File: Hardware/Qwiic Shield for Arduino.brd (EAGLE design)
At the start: 53.3 x 59.7 mm, 22 parts, among them Q1 BSS138, Q2 BSS138, U1 ARDUINO UNO

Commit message: Changed over to Sparkfun library from SparkX
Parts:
- J1, J10, J8, J9: value (none) -> Qwiic Right Angle; device SparkX:1X04_1MM_RA -> SparkFun-Connectors:1X04_1MM_RA
- U$2: value SPARKX-LOGO5 -> SFE_LOGO_NAME_FLAME.1_INCH; device SparkX:SPARKX-LARGE -> SparkFun-Aesthetics:SFE_LOGO_NAME_FLAME_.1
- moved U$2 6.48 mm to (33.0, 1.27)
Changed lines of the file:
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@@
 <grid distance="0.05" unitdist="inch" unit="inch" style="lines" multiple="1" display="yes" altdistance="0.005" altunitdist="inch" altunit="inch"/>
 <layers>
-<layer number="1" name="Top" color="4" fill="1" visible="no" active="yes"/>
+<layer number="1" name="Top" color="4" fill="1" visible="yes" active="yes"/>
 <layer number="2" name="Route2" color="1" fill="3" visible="no" active="no"/>
 <layer number="3" name="Route3" color="4" fill="3" visible="no" active="no"/>
@@
 <layer number="16" name="Bottom" color="1" fill="1" visible="yes" active="yes"/>
 <layer number="17" name="Pads" color="2" fill="1" visible="yes" active="yes"/>
-<layer number="18" name="Vias" color="2" fill="1" visible="yes" active="yes"/>
+<layer number="18" name="Vias" color="2" fill="1" visible="no" active="yes"/>
 <layer number="19" name="Unrouted" color="6" fill="1" visible="no" active="yes"/>
 <layer number="20" name="Dimension" color="15" fill="1" visible="yes" active="yes"/>
 <layer number="21" name="tPlace" color="16" fill="1" visible="yes" active="yes"/>
-<layer number="22" name="bPlace" color="14" fill="1" visible="no" active="yes"/>
+<layer number="22" name="bPlace" color="14" fill="1" visible="yes" active="yes"/>
 <layer number="23" name="tOrigins" color="15" fill="1" visible="yes" active="yes"/>
-<layer number="24" name="bOrigins" color="15" fill="1" visible="no" active="yes"/>
+<layer number="24" name="bOrigins" color="15" fill="1" visible="yes" active="yes"/>
 <layer number="25" name="tNames" color="7" fill="1" visible="no" active="yes"/>
 <layer number="26" name="bNames" color="7" fill="1" visible="no" active="yes"/>
@@
 <element name="FD1" library="SparkFun-Aesthetics" package="FIDUCIAL-1X2" value="FIDUCIAL1X2" x="52.07" y="5.08"/>
 <element name="FD2" library="SparkFun-Aesthetics" package="FIDUCIAL-1X2" value="FIDUCIAL1X2" x="3.81" y="57.15"/>
-<element name="J1" library="SparkX" package="1X04_1MM_RA" value="" x="15.24" y="5.08"/>
+<element name="J1" library="SparkFun-Connectors" package="1X04_1MM_RA" value="Qwiic Right Angle" x="15.24" y="5.08" smashed="yes">
+<attribute name="PROD_ID" value="CONN-13729" x="15.24" y="5.08" size="1.778" layer="27" display="off"/>
+<attribute name="VALUE" value="Qwiic Right Angle" x="15.24" y="5.08" size="1.778" layer="27" display="off"/>
+<attribute name="NAME" x="13.843" y="2.921" size="0.6096" layer="25" font="vector" ratio="20"/>
+<attribute name="VALUE" x="11.049" y="1.778" size="0.6096" layer="27" font="vector" ratio="20"/>
+</element>
 <element name="J2" library="SparkFun-Connectors" package="1X08_NO_SILK" value="" x="7.62" y="54.61" rot="R270">
 <attribute name="PROD_ID" value="CONN-08438" x="7.62" y="54.61" size="1.778" layer="27" font="vector" ratio="15" rot="R270" display="off"/>
@@
 </element>
 <element name="J6" library="SparkFun-Connectors" package="1X07_NO_SILK" value="" x="45.72" y="21.59" rot="R90"/>
-<element name="J8" library="SparkX" package="1X04_1MM_RA" value="" x="22.86" y="5.08"/>
-<element name="J9" library="SparkX" package="1X04_1MM_RA" value="" x="30.48" y="5.08"/>
-<element name="J10" library="SparkX" package="1X04_1MM_RA" value="" x="38.1" y="5.08"/>
-<element name="U$2" library="SparkX" package="SPARKX-LARGE" value="SPARKX-LOGO5" x="26.67" y="2.54" rot="MR0"/>
+<element name="J8" library="SparkFun-Connectors" package="1X04_1MM_RA" value="Qwiic Right Angle" x="22.86" y="5.08" smashed="yes">
+<attribute name="PROD_ID" value="CONN-13729" x="22.86" y="5.08" size="1.778" layer="27" display="off"/>
+<attribute name="VALUE" value="Qwiic Right Angle" x="22.86" y="5.08" size="1.778" layer="27" display="off"/>
+<attribute name="NAME" x="21.463" y="2.921" size="0.6096" layer="25" font="vector" ratio="20"/>
+<attribute name="VALUE" x="18.669" y="0.508" size="0.6096" layer="27" font="vector" ratio="20"/>
+</element>
+<element name="J9" library="SparkFun-Connectors" package="1X04_1MM_RA" value="Qwiic Right Angle" x="30.48" y="5.08" smashed="yes">
+<attribute name="PROD_ID" value="CONN-13729" x="30.48" y="5.08" size="1.778" layer="27" display="off"/>
+<attribute name="VALUE" value="Qwiic Right Angle" x="30.48" y="5.08" size="1.778" layer="27" display="off"/>
+<attribute name="NAME" x="29.083" y="2.921" size="0.6096" layer="25" font="vector" ratio="20"/>
+<attribute name="VALUE" x="26.289" y="1.778" size="0.6096" layer="27" font="vector" ratio="20"/>
+</element>
+<element name="J10" library="SparkFun-Connectors" package="1X04_1MM_RA" value="Qwiic Right Angle" x="38.1" y="5.08" smashed="yes">
+<attribute name="PROD_ID" value="CONN-13729" x="38.1" y="5.08" size="1.778" layer="27" display="off"/>
+<attribute name="VALUE" value="Qwiic Right Angle" x="38.1" y="5.08" size="1.778" layer="27" display="off"/>
+<attribute name="NAME" x="36.703" y="2.921" size="0.6096" layer="25" font="vector" ratio="20"/>
+<attribute name="VALUE" x="33.909" y="0.508" size="0.6096" layer="27" font="vector" ratio="20"/>
+</element>
+<element name="U$2" library="SparkFun-Aesthetics" package="SFE_LOGO_NAME_FLAME_.1" value="SFE_LOGO_NAME_FLAME.1_INCH" x="33.02" y="1.27" rot="MR0"/>
 <element name="U$3" library="SparkX" package="QWIIC_BOARD_MOUNT_HOLES" value="QWIIC_BOARD_OUTLINEH" x="26.67" y="22.86" rot="R90"/>
 <element name="U$1" library="SparkFun-Aesthetics" package="SFE_LOGO_NAME_.1" value="" x="0" y="1.27"/>

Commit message: Partially completed checklist, changes still need to be made
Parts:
- added LOGO2: REVISION, SparkFun-Aesthetics:REVISION
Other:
- board text added: "V01"
- board text removed: "X11"

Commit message: Completed checklist + pre-design review changes
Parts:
- added FD3, FD4: FIDUCIAL1X2, SparkFun-Aesthetics:FIDUCIAL-1X2
- moved LOGO2 31.9 mm to (2.54, -30.5)
- moved FRAME1 3.81 mm to (-8.89, -27.9)
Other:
- board text added: "A. England"
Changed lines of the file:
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@@
 <layer number="23" name="tOrigins" color="15" fill="1" visible="yes" active="yes"/>
 <layer number="24" name="bOrigins" color="15" fill="1" visible="yes" active="yes"/>
-<layer number="25" name="tNames" color="7" fill="1" visible="yes" active="yes"/>
-<layer number="26" name="bNames" color="7" fill="1" visible="yes" active="yes"/>
-<layer number="27" name="tValues" color="7" fill="1" visible="yes" active="yes"/>
-<layer number="28" name="bValues" color="7" fill="1" visible="yes" active="yes"/>
+<layer number="25" name="tNames" color="7" fill="1" visible="no" active="yes"/>
+<layer number="26" name="bNames" color="7" fill="1" visible="no" active="yes"/>
+<layer number="27" name="tValues" color="7" fill="1" visible="no" active="yes"/>
+<layer number="28" name="bValues" color="7" fill="1" visible="no" active="yes"/>
 <layer number="29" name="tStop" color="7" fill="3" visible="yes" active="yes"/>
 <layer number="30" name="bStop" color="7" fill="6" visible="yes" active="yes"/>
@@
 <text x="47.371" y="3.81" size="1.524" layer="21" font="vector" ratio="15" align="center">Qwiic
 Shield</text>
-<text x="22.86" y="-24.13" size="1.778" layer="51" font="vector" ratio="15">N. Seidle</text>
+<text x="21.59" y="-27.94" size="1.778" layer="51" font="vector">N. Seidle</text>
 <wire x1="2.54" y1="0" x2="50.8" y2="0" width="0.2032" layer="20"/>
 <wire x1="0" y1="57.15" x2="2.54" y2="59.69" width="0.2032" layer="20"/>
@@
 <wire x1="53.34" y1="2.54" x2="50.8" y2="0" width="0.2032" layer="20"/>
 <wire x1="2.54" y1="0" x2="0" y2="2.54" width="0.2032" layer="20"/>
-<text x="48.26" y="57.785" size="1.524" layer="16" font="vector" ratio="20" rot="MR0" align="center">V01</text>
 <text x="5.207" y="54.61" size="1.016" layer="21" font="vector" ratio="15" align="center">RX</text>
 <text x="5.207" y="52.07" size="1.016" layer="21" font="vector" ratio="15" align="center">TX</text>
@@
 <text x="27.94" y="26.543" size="1.778" layer="22" font="vector" ratio="15" rot="MR90" align="center">5V</text>
 <text x="25.4" y="25.781" size="1.778" layer="22" font="vector" ratio="15" rot="MR90" align="center">GND</text>
-<text x="26.924" y="8.382" size="1.524" layer="22" font="vector" ratio="15" rot="MR0" align="center">3.3V I C Ports</text>
-<text x="25.781" y="8.636" size="1.016" layer="22" font="vector" ratio="15" rot="MR0">2</text>
 <text x="46.609" y="3.81" size="1.524" layer="22" font="vector" ratio="15" rot="MR0" align="center">Qwiic
 Shield</text>
@@
 <wire x1="17.78" y1="36.83" x2="22.86" y2="36.83" width="1.524" layer="30"/>
 <text x="7.366" y="0.508" size="1.778" layer="16" font="vector" ratio="15" rot="MR0">V01</text>
+<text x="21.59" y="-30.48" size="1.778" layer="51">A. England</text>
+<dimension x1="0" y1="0" x2="0" y2="59.69" x3="-6.35" y3="29.845" textsize="1.778" layer="47"/>
+<dimension x1="0" y1="57.15" x2="0" y2="59.69" x3="-2.54" y3="58.42" textsize="1.778" layer="47"/>
+<dimension x1="0" y1="0" x2="0" y2="2.54" x3="-2.54" y3="1.27" textsize="1.778" layer="47"/>
+<dimension x1="0" y1="0" x2="53.34" y2="0" x3="26.67" y3="-19.05" textsize="1.778" layer="47"/>
+<dimension x1="0" y1="0" x2="2.54" y2="0" x3="1.27" y3="-3.81" textsize="1.778" layer="47"/>
 </plain>
 <attributes>
@@
 <elements>
 <element name="U1" library="SparkFun-Boards" package="UNO_R3_SHIELD_NOLABELS" value="ARDUINO UNO" x="0" y="0"/>
-<element name="FRAME1" library="SparkFun-Aesthetics" package="CREATIVE_COMMONS" value="FRAME-LETTER" x="-8.89" y="-24.13"/>
+<element name="FRAME1" library="SparkFun-Aesthetics" package="CREATIVE_COMMONS" value="FRAME-LETTER" x="-8.89" y="-27.94"/>
 <element name="Q1" library="SparkFun-DiscreteSemi" package="SOT23-3" value="BSS138" x="50.8" y="12.7" smashed="yes">
 <attribute name="NAME" x="49.9745" y="14.478" size="0.8128" layer="25"/>
@@
 <element name="U$3" library="SparkX" package="QWIIC_BOARD_MOUNT_HOLES" value="QWIIC_BOARD_OUTLINEH" x="26.67" y="22.86" rot="R90"/>
 <element name="U$1" library="SparkFun-Aesthetics" package="SFE_LOGO_NAME_.1" value="" x="0" y="1.27"/>
-<element name="LOGO2" library="SparkFun-Aesthetics" package="REVISION" value="REVISION" x="-29.21" y="-27.94"/>
+<element name="LOGO2" library="SparkFun-Aesthetics" package="REVISION" value="REVISION" x="2.54" y="-30.48"/>
+<element name="FD3" library="SparkFun-Aesthetics" package="FIDUCIAL-1X2" value="FIDUCIAL1X2" x="52.07" y="5.08" rot="MR0"/>
+<element name="FD4" library="SparkFun-Aesthetics" package="FIDUCIAL-1X2" value="FIDUCIAL1X2" x="3.81" y="57.15" rot="MR0"/>
 </elements>
 <signals>
@@
 <contactref element="U1" pad="5V"/>
 <contactref element="J6" pad="4"/>
-<wire x1="49.95" y1="15.24" x2="49.95" y2="16.217" width="0.254" layer="1"/>
-<wire x1="49.95" y1="16.217" x2="49.657" y2="16.51" width="0.254" layer="1"/>
-<wire x1="49.657" y1="16.51" x2="46.14" y2="16.51" width="0.254" layer="1"/>
 <wire x1="46.14" y1="15.24" x2="46.14" y2="16.51" width="0.254" layer="1"/>
 <wire x1="46.14" y1="16.51" x2="46.14" y2="18.2" width="0.254" layer="1"/>
@@
 <wire x1="27.94" y1="52.07" x2="29.21" y2="53.34" width="0.254" layer="16"/>
 <wire x1="29.21" y1="53.34" x2="43.18" y2="53.34" width="0.254" layer="16"/>
+<wire x1="49.95" y1="15.24" x2="49.022" y2="15.24" width="0.254" layer="1"/>
+<wire x1="49.022" y1="15.24" x2="48.895" y2="15.367" width="0.254" layer="1"/>
+<wire x1="48.895" y1="15.367" x2="48.895" y2="16.002" width="0.254" layer="1"/>
+<wire x1="48.895" y1="16.002" x2="48.387" y2="16.51" width="0.254" layer="1"/>
+<wire x1="48.387" y1="16.51" x2="46.14" y2="16.51" width="0.254" layer="1"/>
 </signal>
 <signal name="RX">

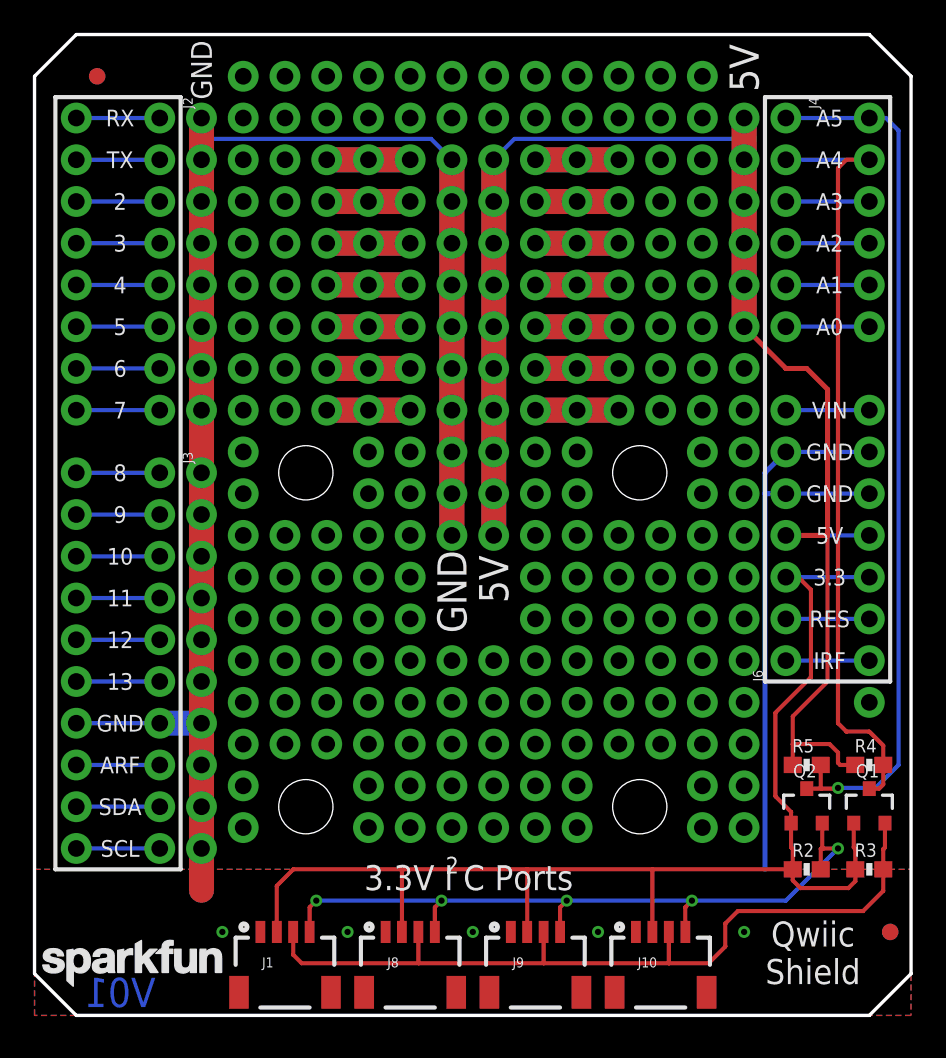
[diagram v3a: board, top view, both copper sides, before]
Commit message: Added mask and silk outline to rails. Added 3.3V Rail
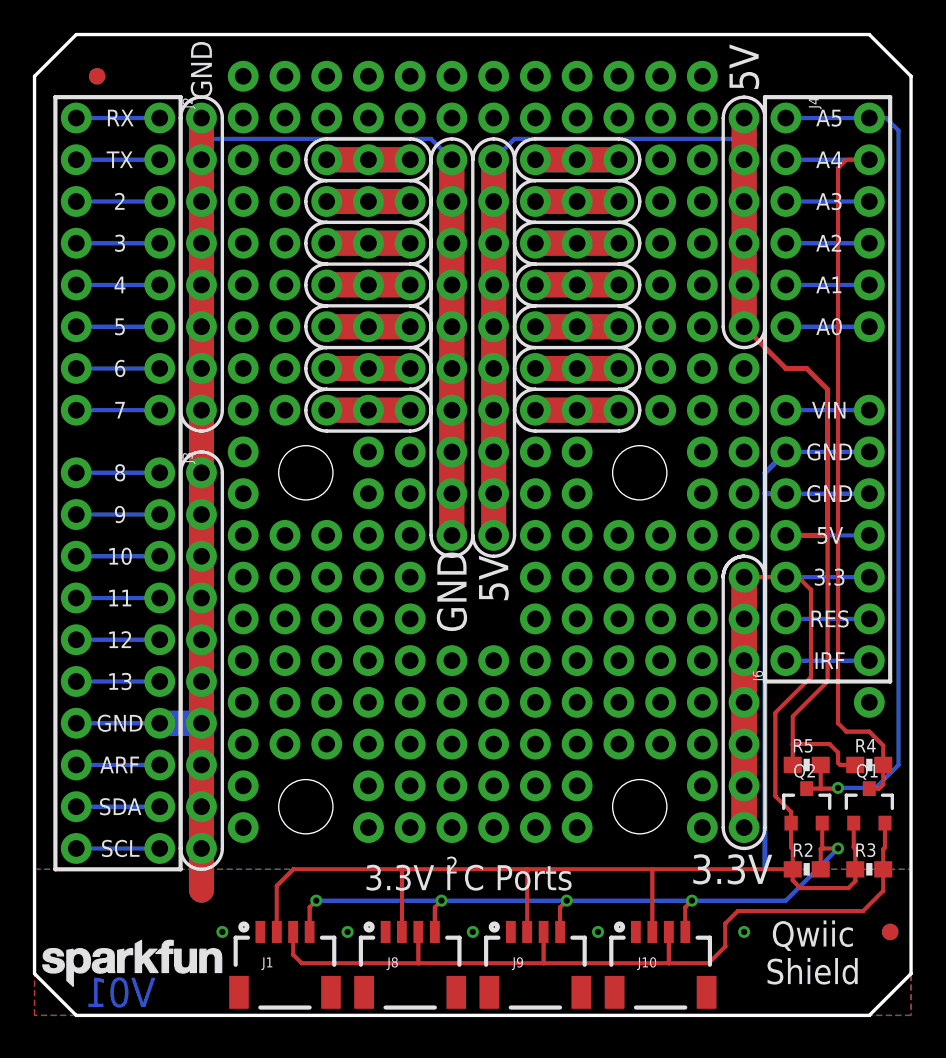
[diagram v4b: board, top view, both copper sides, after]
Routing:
- net 3.3V: track 79.8 -> 128.0 mm, vias 0 -> 2
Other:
- board text added: "3.3V"
